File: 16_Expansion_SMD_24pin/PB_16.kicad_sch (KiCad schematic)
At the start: 10 parts, among them J17 Power In Left, J18 Power In Right, J20 v4 Input

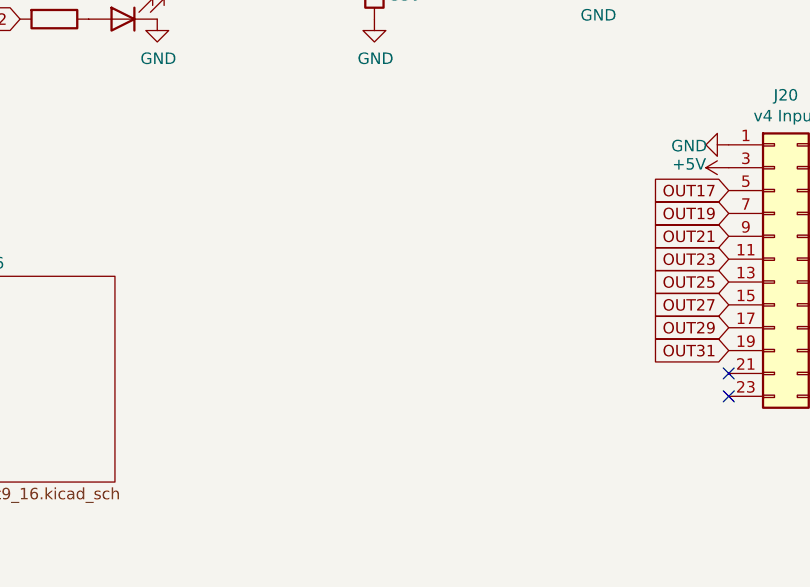
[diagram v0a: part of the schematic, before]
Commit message: added resistors to help with noise the input lines causing flickering, Updated BOMS
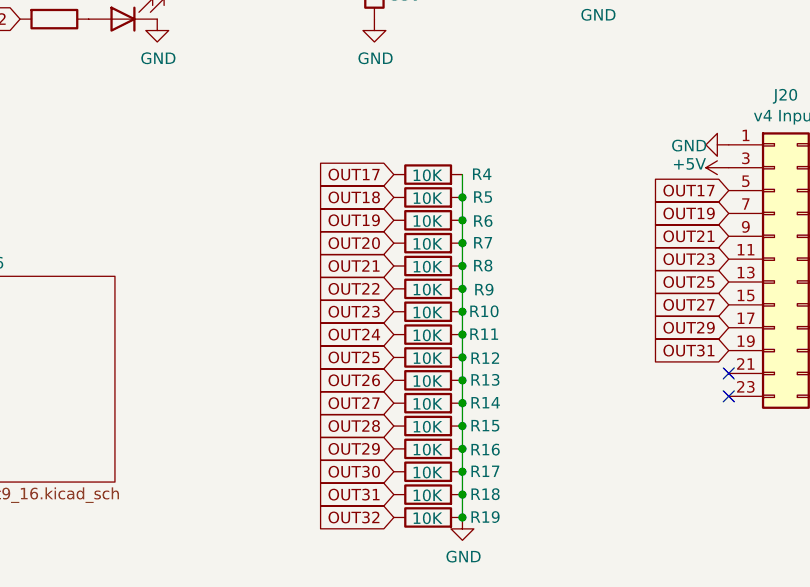
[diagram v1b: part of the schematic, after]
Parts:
- added R10, R11, R12, R13, R14, R15, R16, R17, R18, R19, R4, R5, R6, R7, R8, R9: 10K, Resistor_SMD:R_0603_1608Metric_Pad0.98x0.95mm_HandSolder, symbol Device:R
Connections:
- net GND: now also R10.2, R11.2, R12.2, R13.2, R14.2, R15.2, R16.2, R17.2, R18.2, R19.2, R4.2, R5.2, R6.2, R7.2, R8.2, R9.2
- net OUT17: now also R4.1
- net OUT18: now also R5.1
- net OUT19: now also R6.1
- net OUT20: now also R7.1
- net OUT21: now also R8.1
- net OUT22: now also R9.1
- net OUT23: now also R10.1
- net OUT24: now also R11.1
- net OUT25: now also R12.1
- net OUT26: now also R13.1
- net OUT27: now also R14.1
- net OUT28: now also R15.1
- net OUT29: now also R16.1
- net OUT30: now also R17.1
- net OUT31: now also R18.1
- net OUT32: now also R19.1

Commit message: update 24pin
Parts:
- removed R10, R11, R12, R13, R14, R15, R16, R17, R18, R19, R4, R5, R6, R7, R8, R9: 10K, Resistor_SMD:R_0603_1608Metric_Pad0.98x0.95mm_HandSolder, symbol Device:R
- added H1, H2, H3, H4: MountingHole, Scotts:MountingHole_3.7mm, symbol Mechanical:MountingHole
- D3, D4, D5: footprint LED_SMD:LED_0805_2012Metric_Pad1.15x1.40mm_HandSolder -> LED_SMD:LED_0603_1608Metric; Digi-Key_PN 732-4986-1-ND -> (none); LCSC C2297 -> (none); MPN 150080VS75000 -> (none)
- R1, R2: value 1K -> 2.2K; footprint Resistor_SMD:R_0805_2012Metric_Pad1.15x1.40mm_HandSolder -> Resistor_SMD:R_0603_1608Metric; Digi-Key_PN 311-1.00KCRCT-ND -> (none); LCSC C17513 -> (none); MPN RC0805FR-071KL -> (none)
- R3: footprint Resistor_SMD:R_0805_2012Metric_Pad1.15x1.40mm_HandSolder -> Resistor_SMD:R_0603_1608Metric; Digi-Key_PN 311-330CRCT-ND -> (none); LCSC C17630 -> (none); MPN RC0805FR-07330RL -> (none)
